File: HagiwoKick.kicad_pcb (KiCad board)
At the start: 2 copper layers, 30 x 106 mm, 37 parts, among them J1 TUNECV, J2 OUT, J3 TRIG

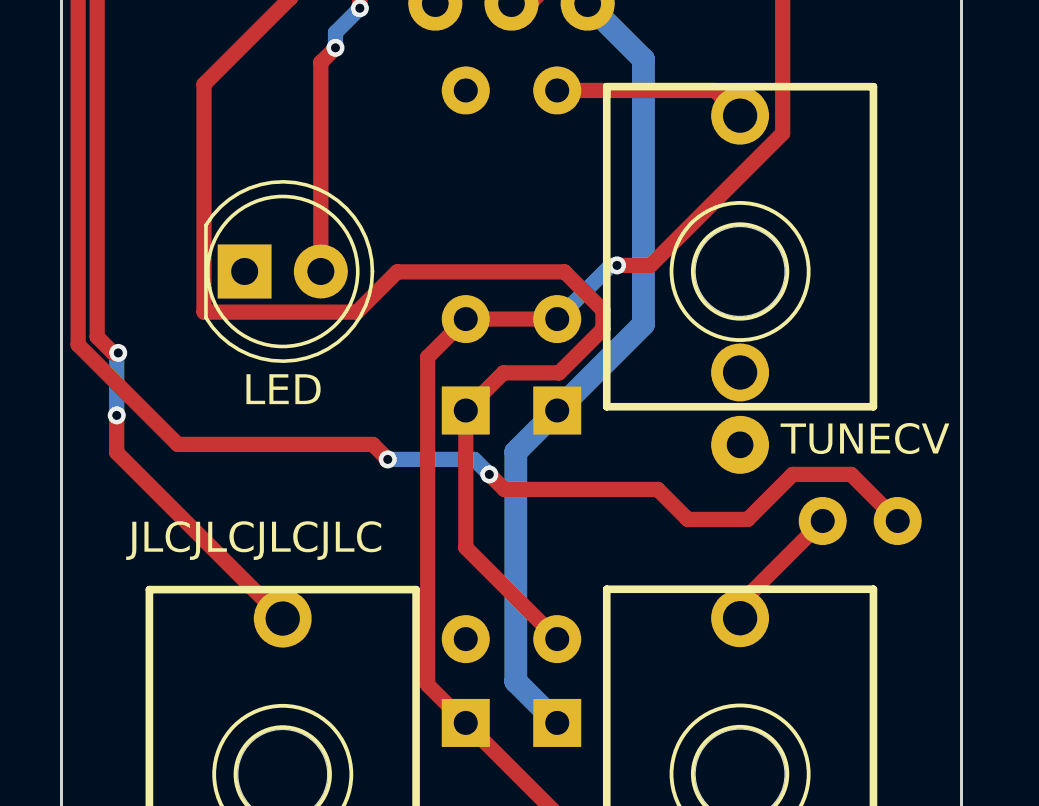
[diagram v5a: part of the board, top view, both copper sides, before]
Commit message: minor repositioning - V1.2 ready for fabrication
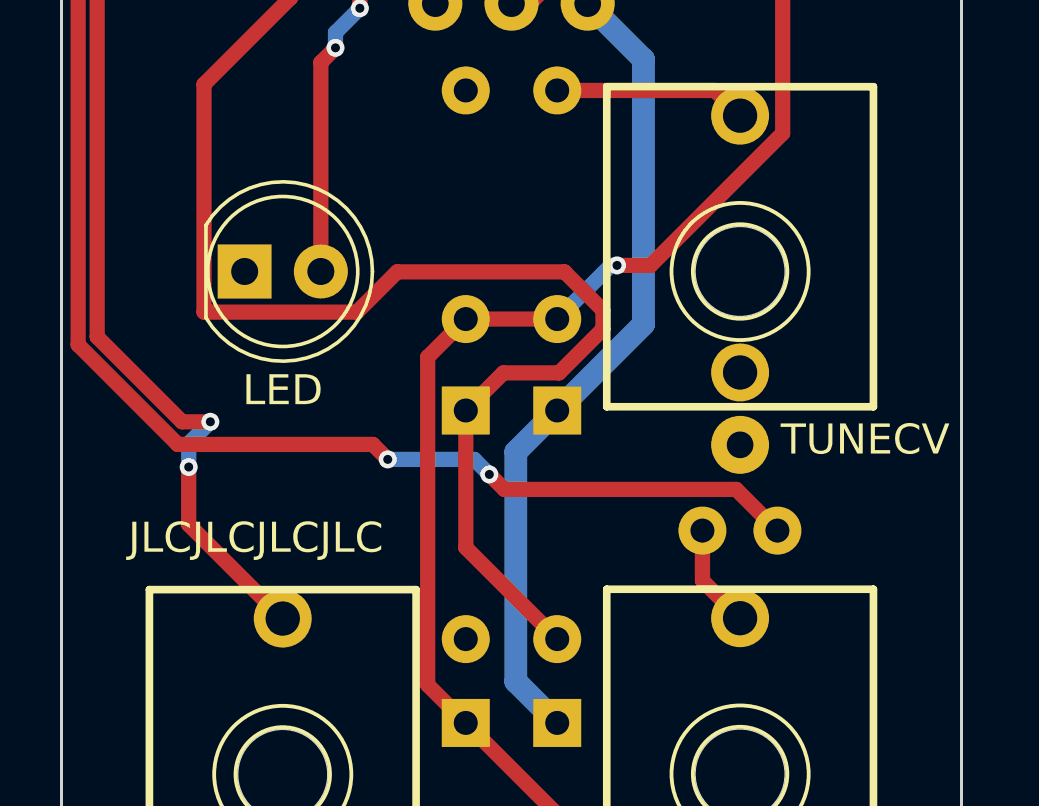
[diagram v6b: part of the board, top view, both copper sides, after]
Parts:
- moved C10 4.02 mm to (74.9, 140.7)
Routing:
- net Net-(C10-Pad1): track 89.4 -> 84.2 mm
- net Net-(J3-SIG): track 42.6 -> 43.6 mm
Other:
- board text added: "SCHEMATIC & CODE BY HAGIWO"
- board text added: "TR KICK"
- board text removed: "`TR KICK` BY HAGIWO"

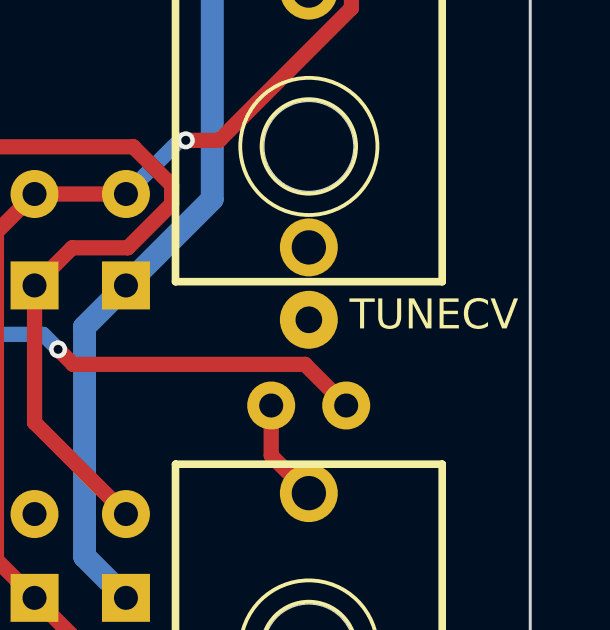
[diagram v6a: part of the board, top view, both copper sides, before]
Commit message: corrected silkscreening issue that TUNE should be TONE and other minor fixed for v1.3
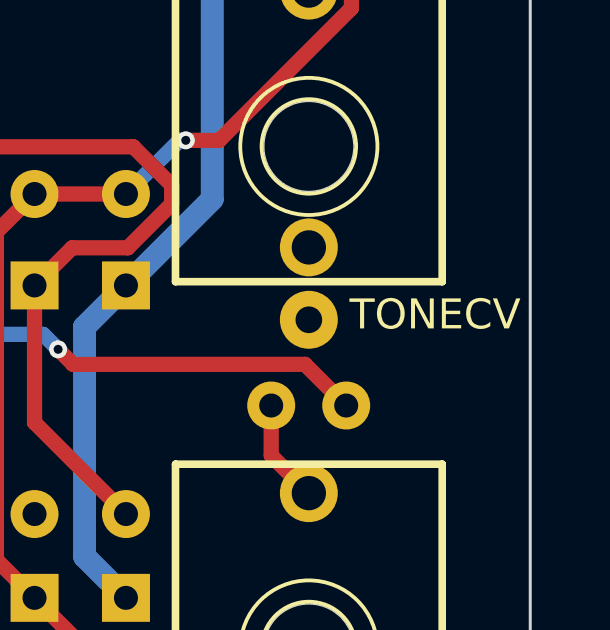
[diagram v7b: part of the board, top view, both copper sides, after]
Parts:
- J1: value TUNECV -> TONECV
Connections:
- J1 pad 2: unconnected-(J1-SHEILD-Pad2) -> GND
- J1 pad 3: GND -> unconnected-(J1-SW-Pad3)
- J2 pad 2: unconnected-(J2-SHEILD-Pad2) -> GND
- J2 pad 3: GND -> unconnected-(J2-SW-Pad3)
- J3 pad 2: unconnected-(J3-SHEILD-Pad2) -> GND
- J3 pad 3: GND -> unconnected-(J3-SW-Pad3)
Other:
- board text added: "V1.3"
- board text removed: "V1.2"
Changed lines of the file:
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@@
 	(net 31 "Net-(C8-Pad1)")
 	(net 32 "Net-(C10-Pad1)")
-	(net 33 "unconnected-(J1-SHEILD-Pad2)")
+	(net 33 "unconnected-(J1-SW-Pad3)")
 	(net 34 "Net-(D7-A)")
 	(net 35 "Net-(J1-SIG)")
-	(net 36 "unconnected-(J2-SHEILD-Pad2)")
+	(net 36 "unconnected-(J2-SW-Pad3)")
 	(net 37 "Net-(J3-SIG)")
-	(net 38 "unconnected-(J3-SHEILD-Pad2)")
+	(net 38 "unconnected-(J3-SW-Pad3)")
 	(net 39 "-12V")
 	(net 40 "Net-(R2-Pad1)")
@@
 			(layers "*.Cu" "*.Mask")
 			(remove_unused_layers no)
-			(net 36 "unconnected-(J2-SHEILD-Pad2)")
+			(net 12 "GND")
 			(pinfunction "SHEILD")
-			(pintype "passive+no_connect")
+			(pintype "passive")
 		)
 		(pad "3" thru_hole circle
@@
 			(layers "*.Cu" "*.Mask")
 			(remove_unused_layers no)
-			(net 12 "GND")
+			(net 36 "unconnected-(J2-SW-Pad3)")
 			(pinfunction "SW")
-			(pintype "passive")
+			(pintype "passive+no_connect")
 		)
 		(model "${KICAD_4MS_LIBS}/3dmodels/Jack.3dshapes/PJ301M-12.WRL"
@@
 			)
 		)
-		(property "Value" "TUNECV"
+		(property "Value" "TONECV"
 			(at 6.1763 -1.355 180)
 			(layer "F.SilkS")
@@
 			(layers "*.Cu" "*.Mask")
 			(remove_unused_layers no)
-			(net 33 "unconnected-(J1-SHEILD-Pad2)")
+			(net 12 "GND")
 			(pinfunction "SHEILD")
-			(pintype "passive+no_connect")
+			(pintype "passive")
 		)
 		(pad "3" thru_hole circle
@@
 			(layers "*.Cu" "*.Mask")
 			(remove_unused_layers no)
-			(net 12 "GND")
+			(net 33 "unconnected-(J1-SW-Pad3)")
 			(pinfunction "SW")
-			(pintype "passive")
+			(pintype "passive+no_connect")
 		)
 		(model "${KICAD_4MS_LIBS}/3dmodels/Jack.3dshapes/PJ301M-12.WRL"
@@
 			(layers "*.Cu" "*.Mask")
 			(remove_unused_layers no)
-			(net 38 "unconnected-(J3-SHEILD-Pad2)")
+			(net 12 "GND")
 			(pinfunction "SHEILD")
-			(pintype "passive+no_connect")
+			(pintype "passive")
 		)
 		(pad "3" thru_hole circle
@@
 			(layers "*.Cu" "*.Mask")
 			(remove_unused_layers no)
-			(net 12 "GND")
+			(net 38 "unconnected-(J3-SW-Pad3)")
 			(pinfunction "SW")
-			(pintype "passive")
+			(pintype "passive+no_connect")
 		)
 		(model "${KICAD_4MS_LIBS}/3dmodels/Jack.3dshapes/PJ301M-12.WRL"
@@
 		)
 	)
-	(gr_text "V1.2"
+	(gr_text "V1.3"
 		(at 54.859 149.3393 270)
 		(layer "B.SilkS" knockout)
